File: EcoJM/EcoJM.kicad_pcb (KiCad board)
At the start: 2 copper layers, 1 part, among them U1 ACS712xLCTR-30A

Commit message: Schematic = 100% , Footprints=100%
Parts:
- added C1: 4.7n, LED_SMD:LED_1206_3216Metric_Pad1.42x1.75mm_HandSolder, F.Cu at (128.7, 100.9)
- added C2: 100n, LED_SMD:LED_1206_3216Metric_Pad1.42x1.75mm_HandSolder, F.Cu at (128.7, 104.3)
- added C3: 22u, LED_SMD:LED_1206_3216Metric_Pad1.42x1.75mm_HandSolder, F.Cu at (128.7, 107.7)
- added C4: 22u, LED_SMD:LED_1206_3216Metric_Pad1.42x1.75mm_HandSolder, F.Cu at (128.7, 111.0)
- added C5: 100n, LED_SMD:LED_1206_3216Metric_Pad1.42x1.75mm_HandSolder, F.Cu at (128.7, 114.4)
- added C6: 22n, LED_SMD:LED_1206_3216Metric_Pad1.42x1.75mm_HandSolder, F.Cu at (128.7, 117.8)
- added C7: 10u, LED_SMD:LED_1206_3216Metric_Pad1.42x1.75mm_HandSolder, F.Cu at (128.7, 121.2)
- added F1: Fuse, Fuse:Fuseholder_Clip-5x20mm_Keystone_3512_Inline_P23.62x7.27mm_D1.02x1.57mm_Horizontal, F.Cu at (110.0, 63.3)
- added J3: Conn_01x02_Pin, Connector_JST:JST_XH_B2B-XH-A_1x02_P2.50mm_Vertical, F.Cu at (107.4, 142.1)
- added J4: Conn_01x02_Pin, Connector_PinHeader_2.54mm:PinHeader_1x02_P2.54mm_Vertical, F.Cu at (143.5, 67.5)
- added J5: Conn_01x03_Pin, Connector_JST:JST_XH_B3B-XH-A_1x03_P2.50mm_Vertical, F.Cu at (73.2, 141.9)
- added J6: Conn_01x02_Pin, Connector_PinHeader_2.54mm:PinHeader_1x02_P2.54mm_Vertical, F.Cu at (71.3, 131.3)
- added J7: Conn_01x03_Pin, Connector_JST:JST_XH_B3B-XH-A_1x03_P2.50mm_Vertical, F.Cu at (89.5, 142.0)
- added J8: Screw_Terminal_01x02, TerminalBlock_Phoenix:TerminalBlock_Phoenix_PT-1,5-2-3.5-H_1x02_P3.50mm_Horizontal, F.Cu at (109.4, 103.7)
- added J9: Screw_Terminal_01x02, TerminalBlock_Phoenix:TerminalBlock_Phoenix_PT-1,5-2-3.5-H_1x02_P3.50mm_Horizontal, F.Cu at (109.8, 78.6)
- added L1: 10u, EasyEDA:IND-SMD_L7.2-W6.6_GPSR07X0, F.Cu at (106.1, 123.2)
- added Q1: 2SD882_C842818, EasyEDA:SOT-89-3_L4.5-W2.5-P1.50-LS4.1-BR, F.Cu at (101.9, 102.0)
- added Q2: 2SD882_C842818, EasyEDA:SOT-89-3_L4.5-W2.5-P1.50-LS4.1-BR, F.Cu at (101.8, 77.3)
- added R1: 10k, Resistor_SMD:R_1206_3216Metric_Pad1.30x1.75mm_HandSolder, F.Cu at (134.7, 100.8)
- added R10: 2.2k, Resistor_SMD:R_1206_3216Metric_Pad1.30x1.75mm_HandSolder, F.Cu at (140.6, 114.1)
- added R11: 47k, Resistor_SMD:R_1206_3216Metric_Pad1.30x1.75mm_HandSolder, F.Cu at (146.6, 100.8)
- added R12: 2.2k, Resistor_SMD:R_1206_3216Metric_Pad1.30x1.75mm_HandSolder, F.Cu at (146.6, 104.2)
- added R13: 470, Resistor_SMD:R_1206_3216Metric_Pad1.30x1.75mm_HandSolder, F.Cu at (146.6, 107.5)
- added R14: 470, Resistor_SMD:R_1206_3216Metric_Pad1.30x1.75mm_HandSolder, F.Cu at (146.6, 110.8)
- added R15: 470, Resistor_SMD:R_1206_3216Metric_Pad1.30x1.75mm_HandSolder, F.Cu at (146.6, 114.1)
- added R2: 10k, Resistor_SMD:R_1206_3216Metric_Pad1.30x1.75mm_HandSolder, F.Cu at (134.7, 104.2)
- added R3: R, Resistor_SMD:R_1206_3216Metric_Pad1.30x1.75mm_HandSolder, F.Cu at (134.7, 107.5)
- added R4: R, Resistor_SMD:R_1206_3216Metric_Pad1.30x1.75mm_HandSolder, F.Cu at (134.7, 110.8)
- added R5: 120, Resistor_SMD:R_1206_3216Metric_Pad1.30x1.75mm_HandSolder, F.Cu at (134.7, 114.1)
- added R6: 10k, Resistor_SMD:R_1206_3216Metric_Pad1.30x1.75mm_HandSolder, F.Cu at (140.6, 100.8)
- added R7: 20k, Resistor_SMD:R_1206_3216Metric_Pad1.30x1.75mm_HandSolder, F.Cu at (140.6, 104.2)
- added R8: 470, Resistor_SMD:R_1206_3216Metric_Pad1.30x1.75mm_HandSolder, F.Cu at (140.6, 107.5)
- added R9: 47k, Resistor_SMD:R_1206_3216Metric_Pad1.30x1.75mm_HandSolder, F.Cu at (140.6, 110.8)
- added U2: MT2492, EasyEDA:SOT-23-6_L2.9-W1.6-P0.95-LS2.8-BL_3, F.Cu at (106.5, 129.9)
- added U3: SIT65HVD230DR, EasyEDA:SOP-8_L4.9-W3.9-P1.27-LS6.0-BL, F.Cu at (77.6, 131.9)
- added U4: AZ1117-3.3, Package_TO_SOT_SMD:SOT-89-3_Handsoldering, F.Cu at (124.6, 142.7)
- added U5: RS321BXF, EasyEDA:SOT-23-5_L2.9-W1.6-P0.95-LS2.8-BL, F.Cu at (86.4, 70.5)
- added U6: STM32F_dev, dev_board:STM32F_devboard, F.Cu at (74.2, 100.5)
- added U7: PC817C_C3025164, EasyEDA:OPTO-SMD-4_L4.6-W6.5-P2.54-LS10.3-TL, F.Cu at (101.9, 86.4)
- added U8: PC817C_C3025164, EasyEDA:OPTO-SMD-4_L4.6-W6.5-P2.54-LS10.3-TL, F.Cu at (101.9, 111.1)
- moved U1 48.4 mm to (78.7, 69.0), turned to -90 degrees
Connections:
- net Net-(U1-IP--Pad3) renamed /VDCH+_OUT
- U1 pad 5: unconnected-(U1-GND-Pad5) -> GND
- U1 pad 6: unconnected-(U1-FILTER-Pad6) -> Net-(U1-FILTER)
- U1 pad 7: unconnected-(U1-VIOUT-Pad7) -> Net-(U1-VIOUT)
- U1 pad 8: unconnected-(U1-VCC-Pad8) -> +5V
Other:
- board outline added: 49.2 x 100.1 mm

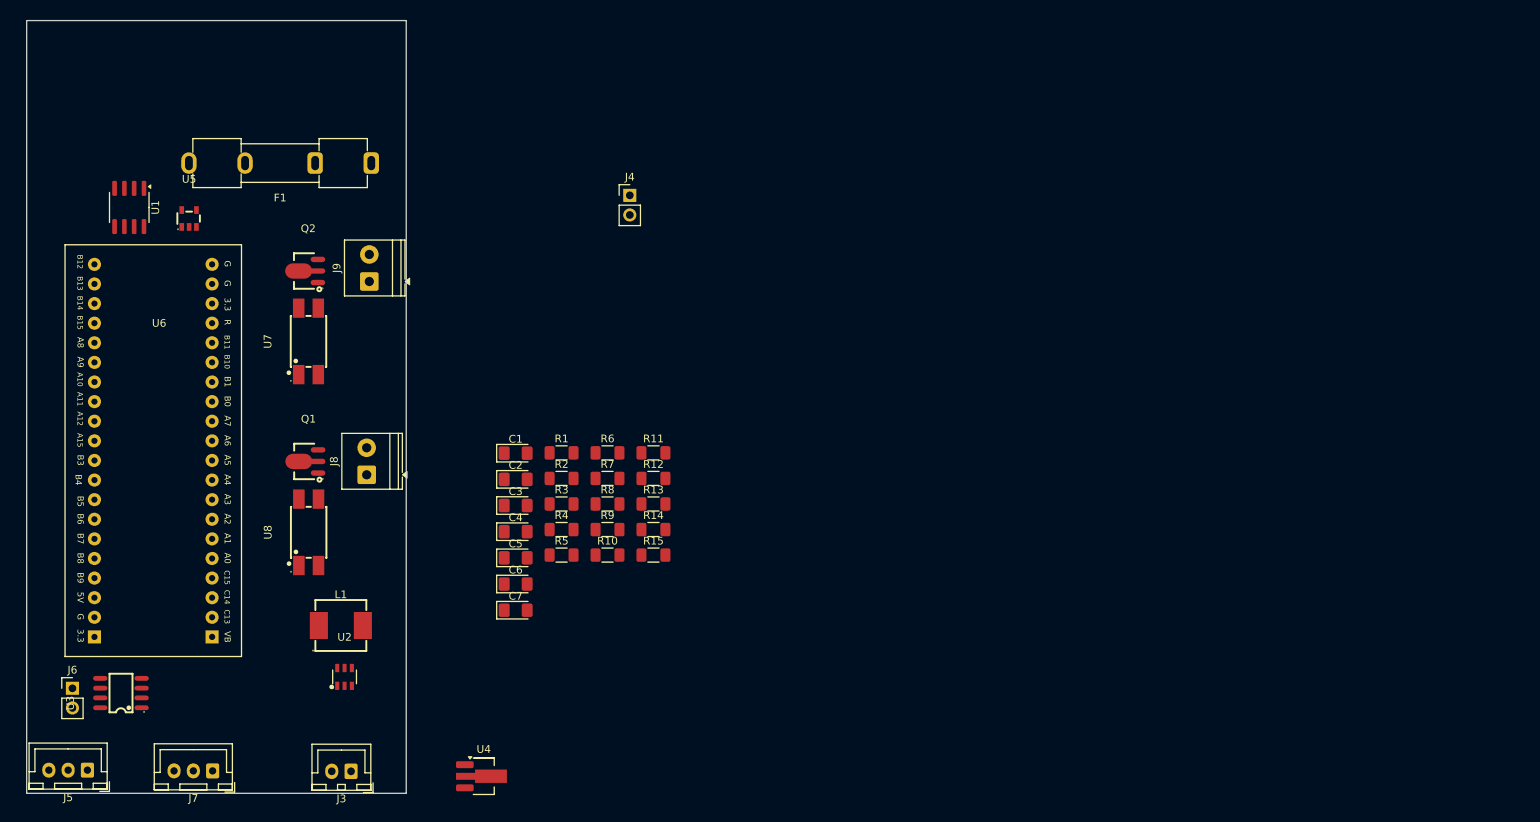
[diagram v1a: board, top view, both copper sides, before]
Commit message: Schematic REV by OMAR_MAGDY , REV0 Layout 80%
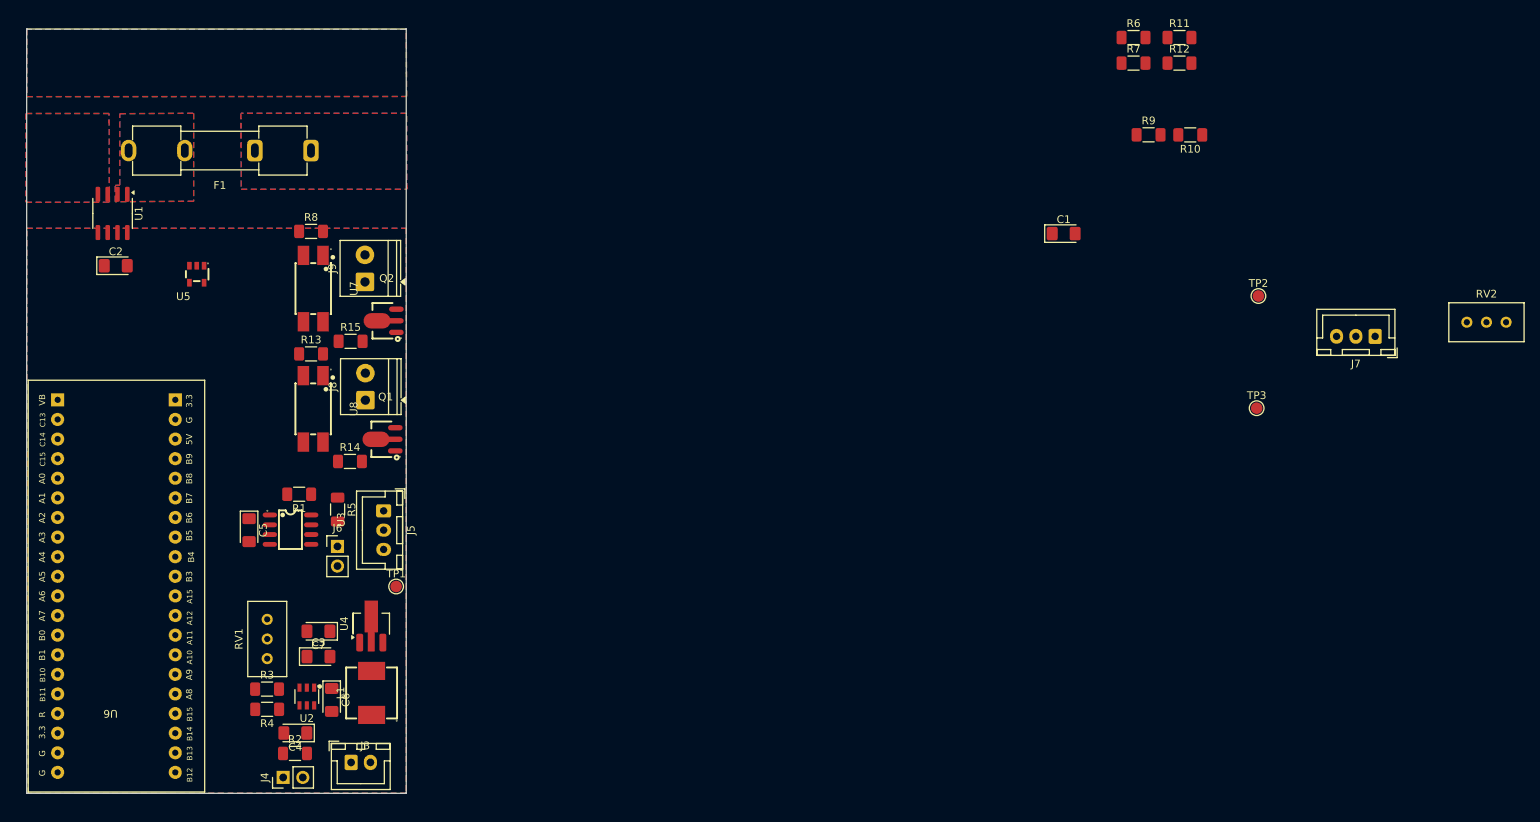
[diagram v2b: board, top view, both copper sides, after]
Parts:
- added RV1: 10k, Potentiometer_THT:Potentiometer_Bourns_3296W_Vertical, F.Cu at (96.5, 122.4)
- added RV2: 10k, Potentiometer_THT:Potentiometer_Bourns_3296W_Vertical, F.Cu at (257.0, 83.9)
- added TP1: TestPoint, TestPoint:TestPoint_Pad_D1.5mm, F.Cu at (113.2, 118.2)
- added TP2: TestPoint, TestPoint:TestPoint_Pad_D1.5mm, F.Cu at (224.9, 80.5)
- added TP3: TestPoint, TestPoint:TestPoint_Pad_D1.5mm, F.Cu at (224.7, 95.0)
- R14, R15: value 470 -> 100
- R3: value R -> 68k
- R4: value R -> 10k
- moved J7 160.8 mm to (240.1, 85.8)
- moved R10 93.1 mm to (216.1, 59.6), turned to 180 degrees
- moved J4 87.8 mm to (98.6, 142.9), turned to 90 degrees
- moved R11 86.8 mm to (214.7, 47.0)
- moved R12 86.8 mm to (214.7, 50.4)
- moved R6 86.8 mm to (208.8, 47.0)
- moved R7 86.8 mm to (208.8, 50.4)
- moved R9 86.8 mm to (210.7, 59.6)
- moved C1 76.5 mm to (199.7, 72.4)
- moved C2 58.7 mm to (76.9, 76.6)
- moved R8 52.2 mm to (102.2, 72.2)
- moved J5 51.0 mm to (111.6, 108.3), turned to -90 degrees
- moved R2 49.6 mm to (100.1, 139.8)
- moved R13 48.4 mm to (102.2, 88.0)
- moved R15 48.0 mm to (107.3, 86.4)
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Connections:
- R12 pad 1: GND -> Net-(R12-Pad1)
- R3 pad 1: +5V -> Net-(R3-Pad1)
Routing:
- added copper zone on B.Cu, net /VDCH+_IN
- added copper zone on F.Cu, net /VDCH+_IN
- added copper zone on B.Cu, net /VDCH+_OUT
- added copper zone on F.Cu, net /VDCH+_OUT
- added copper zone on B.Cu, net /VDCH-
- added copper zone on F.Cu, net /VDCH-
- added copper zone on B.Cu, net GND
- added copper zone on F.Cu, net GND
- added copper zone on B.Cu, net Net-(F1-Pad2)
- added copper zone on F.Cu, net Net-(F1-Pad2)
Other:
- board size 49.2 x 100.1 mm -> 49.2 x 99 mm

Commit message: update
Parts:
- added J1: Conn_01x01_Pin, Connector_Wire:SolderWirePad_1x01_SMD_5x10mm, F.Cu at (109.0, 61.7)
- added J10: Conn_01x01_Pin, Connector_Wire:SolderWirePad_1x01_SMD_5x10mm, F.Cu at (68.8, 62.5)
- added J11: Conn_01x01_Pin, Connector_Wire:SolderWirePad_1x01_SMD_5x10mm, F.Cu at (71.2, 50.3)
- added J2: Conn_01x01_Pin, Connector_Wire:SolderWirePad_1x01_SMD_5x10mm, F.Cu at (108.8, 50.2)
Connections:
- U6 pad 12: unconnected-(U6-B4-Pad12) -> /SSR1
- U6 pad 13: unconnected-(U6-B5-Pad13) -> /SSR0
- U6 pad 27: /SSR1 -> unconnected-(U6-B1-Pad27)
- U6 pad 28: /SSR0 -> unconnected-(U6-B0-Pad28)

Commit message: Routing Finished
bhbk ya Omar ya Magdy
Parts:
- moved J7 171.6 mm to (68.5, 87.0), turned to 90 degrees
- moved RV2 165.0 mm to (92.0, 84.5), turned to 90 degrees
- moved TP2 151.0 mm to (74.0, 78.0)
- moved TP3 141.7 mm to (83.5, 83.0)
- moved R7 135.5 mm to (77.2, 83.0), turned to -90 degrees
- moved R6 134.8 mm to (77.2, 76.5), turned to -90 degrees
- moved R10 134.2 mm to (83.0, 76.8), turned to 0 degrees
- moved C1 129.2 mm to (70.5, 75.0), turned to 180 degrees
- moved R12 124.7 mm to (93.5, 79.5), turned to 180 degrees
- moved R11 124.6 mm to (93.6, 76.5), turned to 180 degrees
- moved R9 123.4 mm to (88.0, 73.0), turned to 180 degrees
- moved C2 6.65 mm to (82.5, 73.0), turned to 180 degrees
- moved R2 3.03 mm to (100.1, 136.8)
- moved C4 2.38 mm to (100.2, 139.5)
- moved C7 1.45 mm to (103.2, 122.5)
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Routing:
- net +5V: track 0.00 -> 103.4 mm, vias 0 -> 6
- net +3.3V: track 0.00 -> 73.5 mm, vias 0 -> 8
- net /SSR0: track 0.00 -> 55.7 mm, vias 0 -> 4
- net /Voltage_M: track 0.00 -> 49.7 mm, vias 0 -> 6
- net /Current_M: track 0.00 -> 43.2 mm, vias 0 -> 3
- net /SSR1: track 0.00 -> 42.3 mm, vias 0 -> 4
- net /VDCH-: track 0.00 -> 42.1 mm, vias 0 -> 2
- net /UART_TX: track 0.00 -> 38.4 mm, vias 0 -> 2
- net /UART_RX: track 0.00 -> 38.3 mm, vias 0 -> 2
- net /CAN_RXD: track 0.00 -> 20.8 mm, vias 0 -> 2
- net /CAN_TXD: track 0.00 -> 19.6 mm, vias 0 -> 2
- net /CAN_L: track 0.00 -> 18.1 mm, vias 0 -> 4
- net /VDCH+_IN: track 0.00 -> 18.0 mm, vias 0 -> 2
- net Net-(J4-Pin_1): track 0.00 -> 17.3 mm, vias 0 -> 4
- net Net-(J9-Pin_1): track 0.00 -> 16.0 mm, vias 0 -> 2
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
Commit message: nseet a3ml save
sorry
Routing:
- net Net-(J6-Pin_1): track 0.00 -> 3.24 mm
- net Net-(U2-BS): track 0.00 -> 2.31 mm
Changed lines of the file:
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@@
+	)
+	(segment
+		(start 102.61 131.255)
+		(end 104.775 131.255)
+		(width 0.2)
+		(layer "F.Cu")
+		(net 41)
+	)
+	(segment
+		(start 104.775 131.255)
+		(end 104.88 131.36)
+		(width 0.2)
+		(layer "F.Cu")
+		(net 41)
 	)
 	(segment
@@
 	)
 	(segment
+		(start 105.63 109.75)
+		(end 105.65 109.73)
+		(width 0.2)
+		(layer "F.Cu")
+		(net 64)
+	)
+	(segment
+		(start 105.63 112.96)
+		(end 105.63 109.75)
+		(width 0.2)
+		(layer "F.Cu")
+		(net 64)
+	)
+	(segment
